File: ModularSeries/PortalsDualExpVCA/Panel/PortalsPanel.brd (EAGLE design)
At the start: 50.5 x 128.5 mm, 14 parts

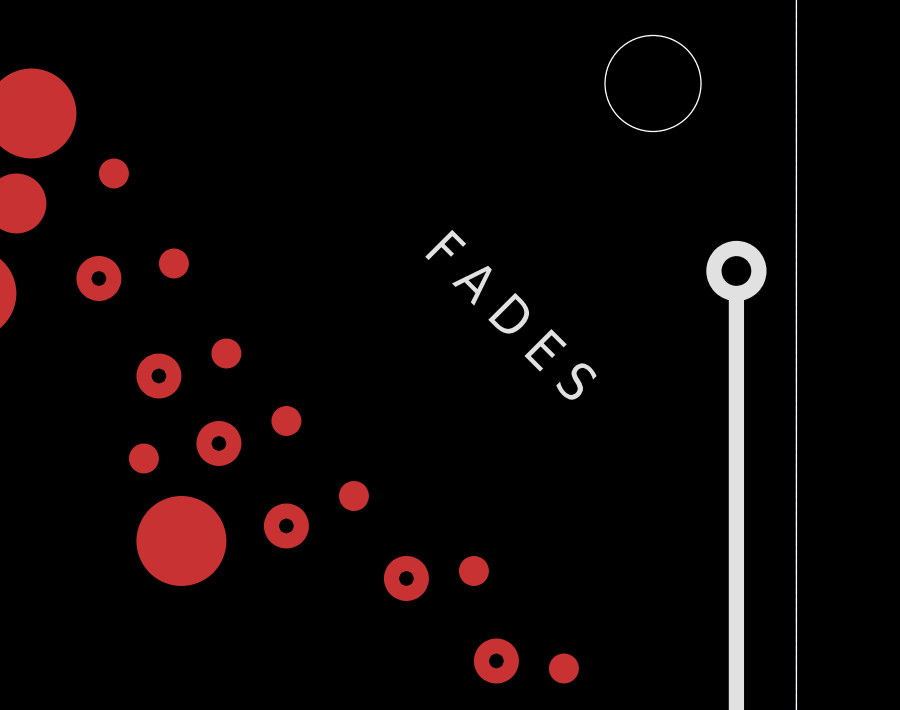
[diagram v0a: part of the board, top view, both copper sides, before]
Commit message: Panel for TimeSeeds added. TLHP core PCB added
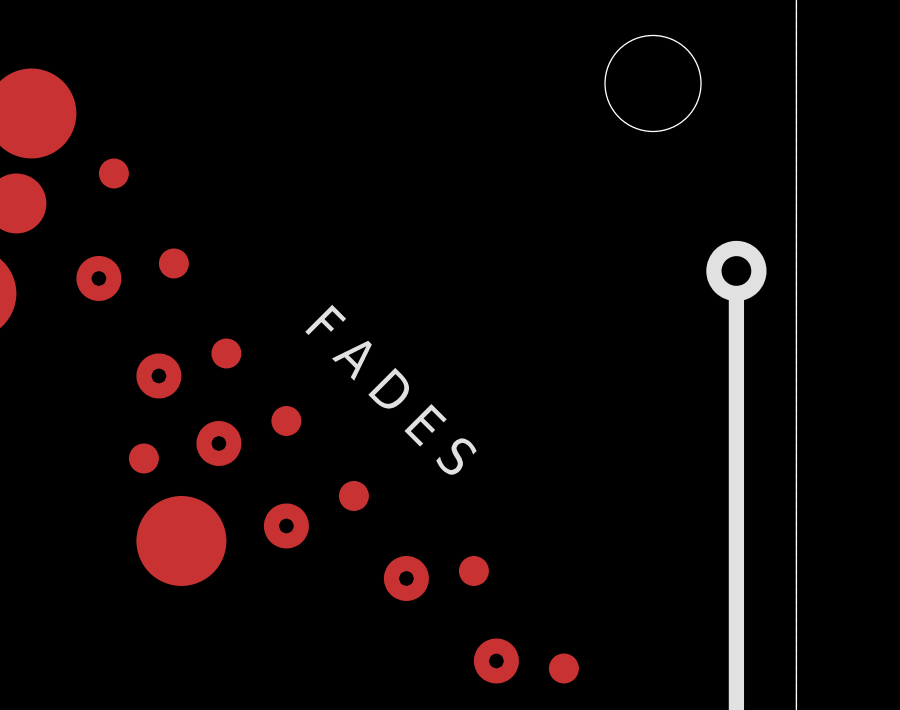
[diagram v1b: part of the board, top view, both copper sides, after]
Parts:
- added E$15: (no value), ElectricNoodleBox:LOGO20X20
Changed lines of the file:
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@@
 <?xml version="1.0" encoding="utf-8"?>
 <!DOCTYPE eagle SYSTEM "eagle.dtd">
-<eagle version="9.6.0">
+<eagle version="9.6.2">
 <drawing>
 <settings>
@@
 <layer number="21" name="tPlace" color="7" fill="1" visible="yes" active="yes"/>
 <layer number="22" name="bPlace" color="7" fill="1" visible="no" active="yes"/>
-<layer number="23" name="tOrigins" color="15" fill="1" visible="no" active="yes"/>
-<layer number="24" name="bOrigins" color="15" fill="1" visible="no" active="yes"/>
+<layer number="23" name="tOrigins" color="15" fill="1" visible="yes" active="yes"/>
+<layer number="24" name="bOrigins" color="15" fill="1" visible="yes" active="yes"/>
 <layer number="25" name="tNames" color="7" fill="1" visible="no" active="yes"/>
 <layer number="26" name="bNames" color="7" fill="1" visible="no" active="yes"/>
@@
 </layers>
 <board>
-<fusionsync huburn="a.cGVyc29uYWw6dWUyYjdlNGE0" projecturn="a.cGVyc29uYWw6dWUyYjdlNGE0IzIwMjAwNDA1MjgzMzA0MTgx" f3durn="urn:adsk.wipprod:dm.lineage:Ls8VfWaLSve3wBAX8ZaC_Q" pcbguid="0b438140-d98a-4172-bfc0-4c50ea6e3d9a" lastpulledtime="" lastsyncedchangeguid="" latestrevisionid="b6e3ded7-6532-4d29-bdbf-7cce59401ae7" lastsyncedrevisionid="b6e3ded7-6532-4d29-bdbf-7cce59401ae7" lastboardhashguid="ee64bccb-d335-b1c3-ee69-583b01692caa" lastpushedtime="2020-06-18T10:11:24Z" linktopcb3d="%12"/>
+<fusionsync huburn="a.cGVyc29uYWw6dWUyYjdlNGE0" projecturn="a.cGVyc29uYWw6dWUyYjdlNGE0IzIwMjAwNDA1MjgzMzA0MTgx" f3durn="urn:adsk.wipprod:dm.lineage:Ls8VfWaLSve3wBAX8ZaC_Q" pcbguid="0b438140-d98a-4172-bfc0-4c50ea6e3d9a" lastpulledtime="" lastsyncedchangeguid="" latestrevisionid="b6e3ded7-6532-4d29-bdbf-7cce59401ae7" lastsyncedrevisionid="b6e3ded7-6532-4d29-bdbf-7cce59401ae7" lastboardhashguid="ee64bccb-d335-b1c3-ee69-583b01692caa" lastpushedtime="2020-06-18T10:11:24Z" linktopcb3d="true"/>
 <plain>
 <wire x1="0" y1="-14.25" x2="50.5" y2="-14.25" width="0" layer="20"/>
@@
 <circle x="38.5" y="31.5" radius="0.25" width="0.5" layer="29"/>
 <circle x="32.5" y="13.75" radius="0.25" width="0.5" layer="29"/>
-<text x="41" y="103.5" size="1.27" layer="21" font="vector" ratio="16" rot="R135" align="center">F A D E S</text>
+<text x="37" y="101" size="1.27" layer="21" font="vector" ratio="16" rot="R135" align="center">F A D E S</text>
 <text x="4.25" y="97.75" size="1.27" layer="21" font="vector" ratio="16" rot="R75" align="center">S I L E N C E S</text>
 <text x="4.25" y="2.25" size="1.27" layer="21" font="vector" ratio="16" rot="R285" align="center">D Y N A M I C S</text>
@@
 <element name="E$13" library="ElectricNoodleBox" package="ALPHA9MM_POT_CUTOUT" value="" x="35" y="39" smashed="yes"/>
 <element name="E$14" library="ElectricNoodleBox" package="ALPHA9MM_POT_CUTOUT" value="" x="39.5" y="17" smashed="yes"/>
+<element name="E$15" library="ElectricNoodleBox" package="LOGO20X20" value="" x="45.75" y="92" smashed="yes" rot="MR0"/>
 </elements>
 <signals>

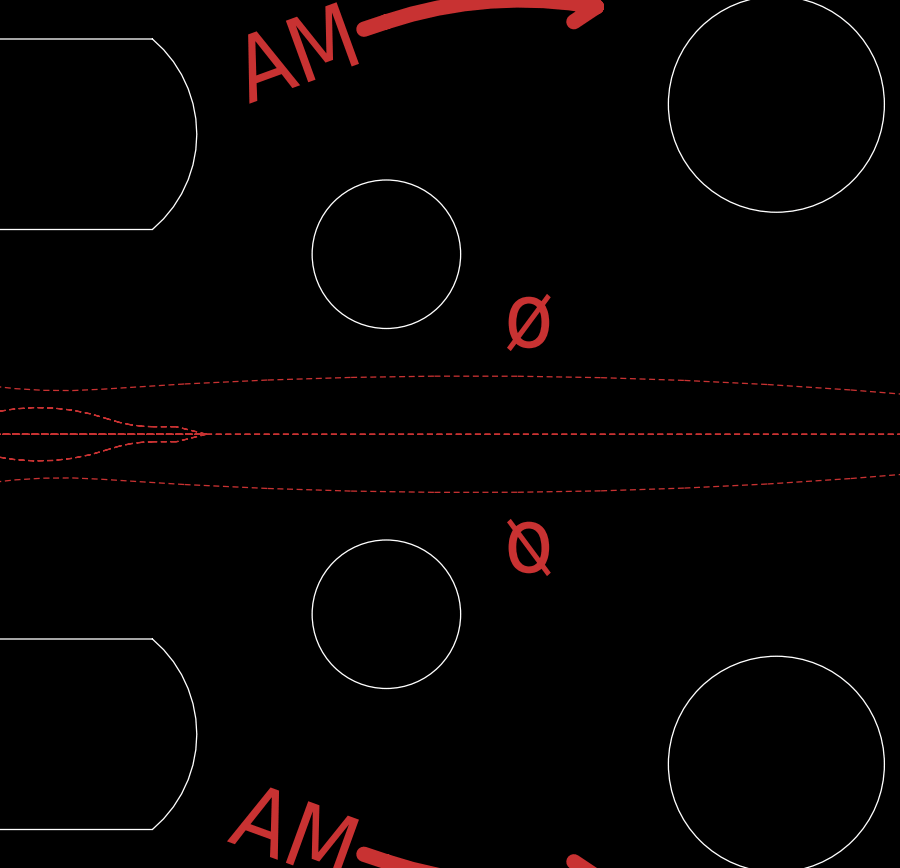
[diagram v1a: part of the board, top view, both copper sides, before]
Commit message: Mirrors and Portals Renders brought up to date
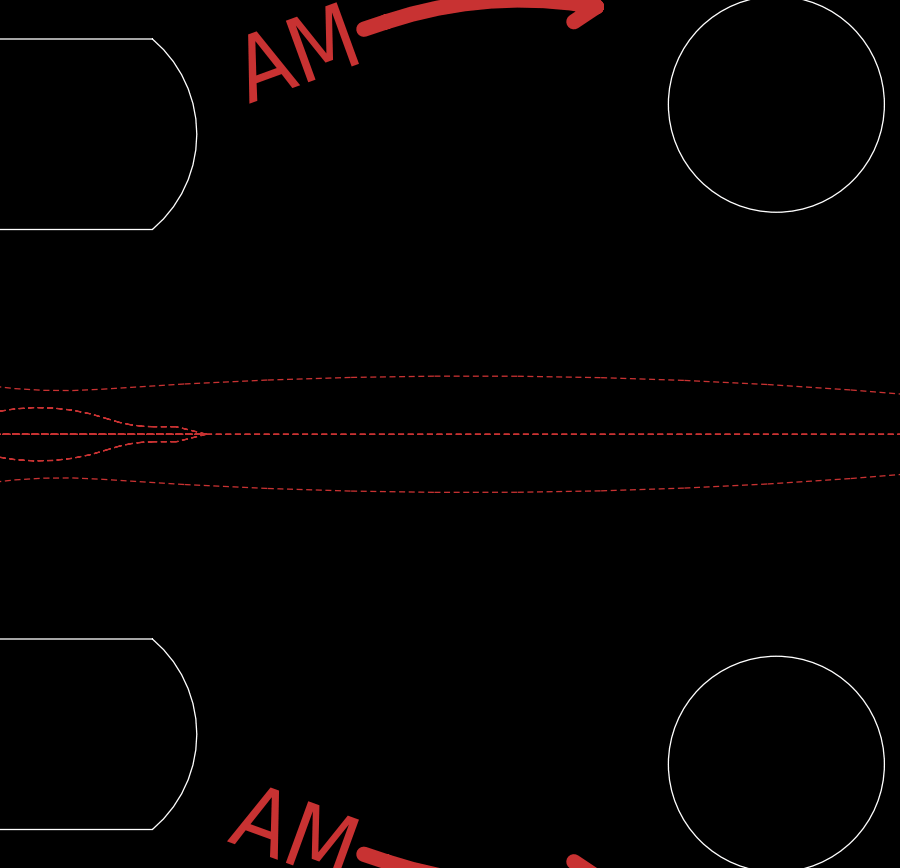
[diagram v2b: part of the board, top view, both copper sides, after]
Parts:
- removed E$10, E$9: (no value), ElectricNoodleBox:DW1_SWITCH_CUTOUT
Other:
- board text removed: "ø"
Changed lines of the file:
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@@
 </layers>
 <board>
-<fusionsync huburn="a.cGVyc29uYWw6dWUyYjdlNGE0" projecturn="a.cGVyc29uYWw6dWUyYjdlNGE0IzIwMjAwNDA1MjgzMzA0MTgx" f3durn="urn:adsk.wipprod:dm.lineage:Ls8VfWaLSve3wBAX8ZaC_Q" pcbguid="0b438140-d98a-4172-bfc0-4c50ea6e3d9a" lastpulledtime="" lastsyncedchangeguid="" latestrevisionid="b6e3ded7-6532-4d29-bdbf-7cce59401ae7" lastsyncedrevisionid="b6e3ded7-6532-4d29-bdbf-7cce59401ae7" lastboardhashguid="ee64bccb-d335-b1c3-ee69-583b01692caa" lastpushedtime="2020-06-18T10:11:24Z" linktopcb3d="true"/>
+<fusionsync huburn="a.cGVyc29uYWw6dWUyYjdlNGE0" projecturn="a.cGVyc29uYWw6dWUyYjdlNGE0IzIwMjAwNDA1MjgzMzA0MTgx" f3durn="urn:adsk.wipprod:dm.lineage:Ls8VfWaLSve3wBAX8ZaC_Q" pcbguid="" lastpulledtime="" lastsyncedchangeguid="" latestrevisionid="b6e3ded7-6532-4d29-bdbf-7cce59401ae7" lastsyncedrevisionid="b6e3ded7-6532-4d29-bdbf-7cce59401ae7" lastboardhashguid="ee64bccb-d335-b1c3-ee69-583b01692caa" lastpushedtime="2020-06-18T10:11:24Z" linktopcb3d="true"/>
 <plain>
 <wire x1="0" y1="-14.25" x2="50.5" y2="-14.25" width="0" layer="20"/>
@@
 <text x="19" y="62.75" size="2.1844" layer="1" font="vector" ratio="16" rot="R20" align="center">AM</text>
 <text x="31.75" y="71.75" size="2.54" layer="1" font="vector" ratio="16" rot="R35" align="center">BIAS</text>
-<text x="26.75" y="54" size="2.1844" layer="1" font="vector" ratio="16" align="center">ø</text>
 <text x="15.75" y="-3" size="2.54" layer="1" font="vector" ratio="16" rot="R335" align="center">OUT</text>
 <text x="5.25" y="27.5" size="2.1844" layer="1" font="vector" ratio="16" rot="R270" align="center">IN</text>
@@
 <text x="19" y="36.75" size="2.1844" layer="1" font="vector" ratio="16" rot="R340" align="center">AM</text>
 <text x="31.75" y="27.75" size="2.54" layer="1" font="vector" ratio="16" rot="R325" align="center">BIAS</text>
-<text x="26.75" y="46.5" size="2.1844" layer="1" font="vector" ratio="16" rot="MR0" align="center">ø</text>
 <polygon width="0.1" layer="29">
 <vertex x="15" y="50.25"/>
@@
 <element name="E$7" library="ElectricNoodleBox" package="CINCH_BANANA_CUTOUT" value="" x="22" y="25" smashed="yes"/>
 <element name="E$8" library="ElectricNoodleBox" package="CINCH_BANANA_CUTOUT" value="" x="18.5" y="5" smashed="yes" rot="R90"/>
-<element name="E$9" library="ElectricNoodleBox" package="DW1_SWITCH_CUTOUT" value="" x="22" y="56" smashed="yes"/>
-<element name="E$10" library="ElectricNoodleBox" package="DW1_SWITCH_CUTOUT" value="" x="22" y="44" smashed="yes"/>
 <element name="E$11" library="ElectricNoodleBox" package="ALPHA9MM_POT_CUTOUT" value="" x="39.5" y="83" smashed="yes"/>
 <element name="E$12" library="ElectricNoodleBox" package="ALPHA9MM_POT_CUTOUT" value="" x="35" y="61" smashed="yes"/>
